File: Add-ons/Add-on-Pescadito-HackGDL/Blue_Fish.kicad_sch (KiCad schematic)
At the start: 16 parts, among them J3 Conn_02x03_Odd_Even, SW5 SW_RST, SW6 On, U3 PY32F002AA15M6TU

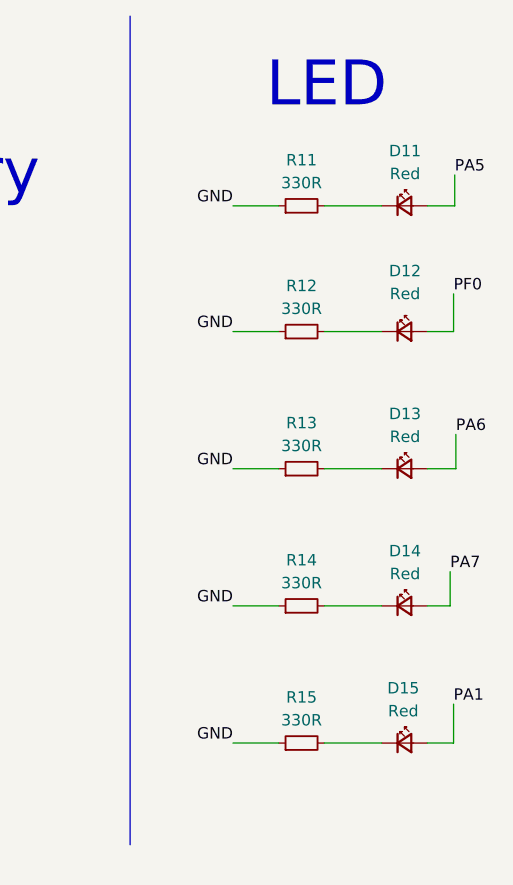
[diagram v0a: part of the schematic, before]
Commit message: feat(Hw):Update_Labels
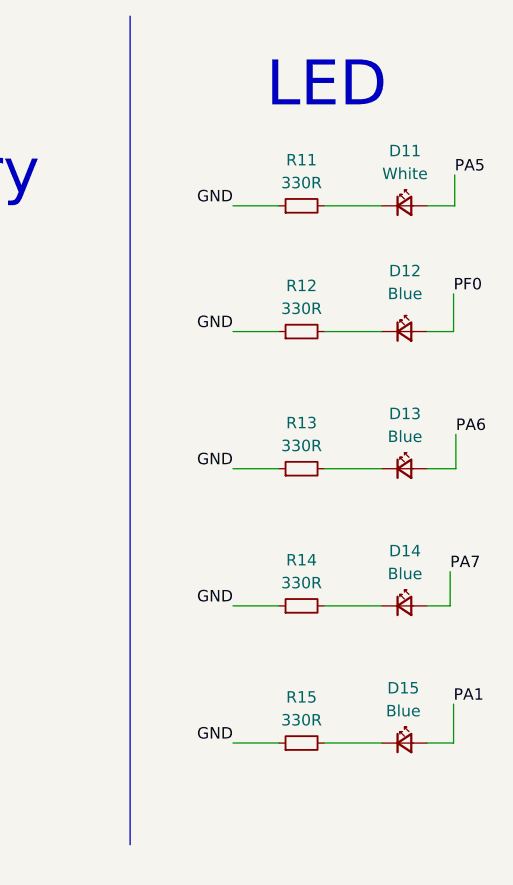
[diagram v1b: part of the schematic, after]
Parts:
- D11: value Red -> White; LCSC# C965812 -> C84258
- D12, D13, D14, D15: value Red -> Blue; LCSC# C965812 -> C205441
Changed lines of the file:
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@@
 			)
 		)
-		(property "Value" "Red"
+		(property "Value" "Blue"
 			(at 184.2135 73.914 0)
 			(effects
@@
 			)
 		)
-		(property "LCSC#" "C965812"
+		(property "LCSC#" "C205441"
 			(at 184.15 77.47 0)
 			(effects
@@
 			)
 		)
-		(property "Value" "Red"
+		(property "Value" "White"
 			(at 184.2135 29.464 0)
 			(effects
@@
 			)
 		)
-		(property "LCSC#" "C965812"
+		(property "LCSC#" "C84258"
 			(at 184.15 33.02 0)
 			(effects
@@
 			)
 		)
-		(property "Value" "Red"
+		(property "Value" "Blue"
 			(at 184.2135 42.799 0)
 			(effects
@@
 			)
 		)
-		(property "LCSC#" "C965812"
+		(property "LCSC#" "C205441"
 			(at 184.15 46.99 0)
 			(effects
@@
 			)
 		)
-		(property "Value" "Red"
+		(property "Value" "Blue"
 			(at 184.023 89.154 0)
 			(effects
@@
 			)
 		)
-		(property "LCSC#" "C965812"
+		(property "LCSC#" "C205441"
 			(at 184.15 92.71 0)
 			(effects
@@
 			)
 		)
-		(property "Value" "Red"
+		(property "Value" "Blue"
 			(at 184.2135 58.674 0)
 			(effects
@@
 			)
 		)
-		(property "LCSC#" "C965812"
+		(property "LCSC#" "C205441"
 			(at 184.15 62.23 0)
 			(effects
